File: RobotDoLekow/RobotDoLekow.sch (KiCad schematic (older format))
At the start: 24 parts, among them M1 Stepper_Motor_unipolar_5pin, Q1 2N3904, SW1 SW_Push_LED, U1 Converter_module, U2 RTC_module_DS1307, U3 ESP8266_module, U4 Driver_module_ULN2003

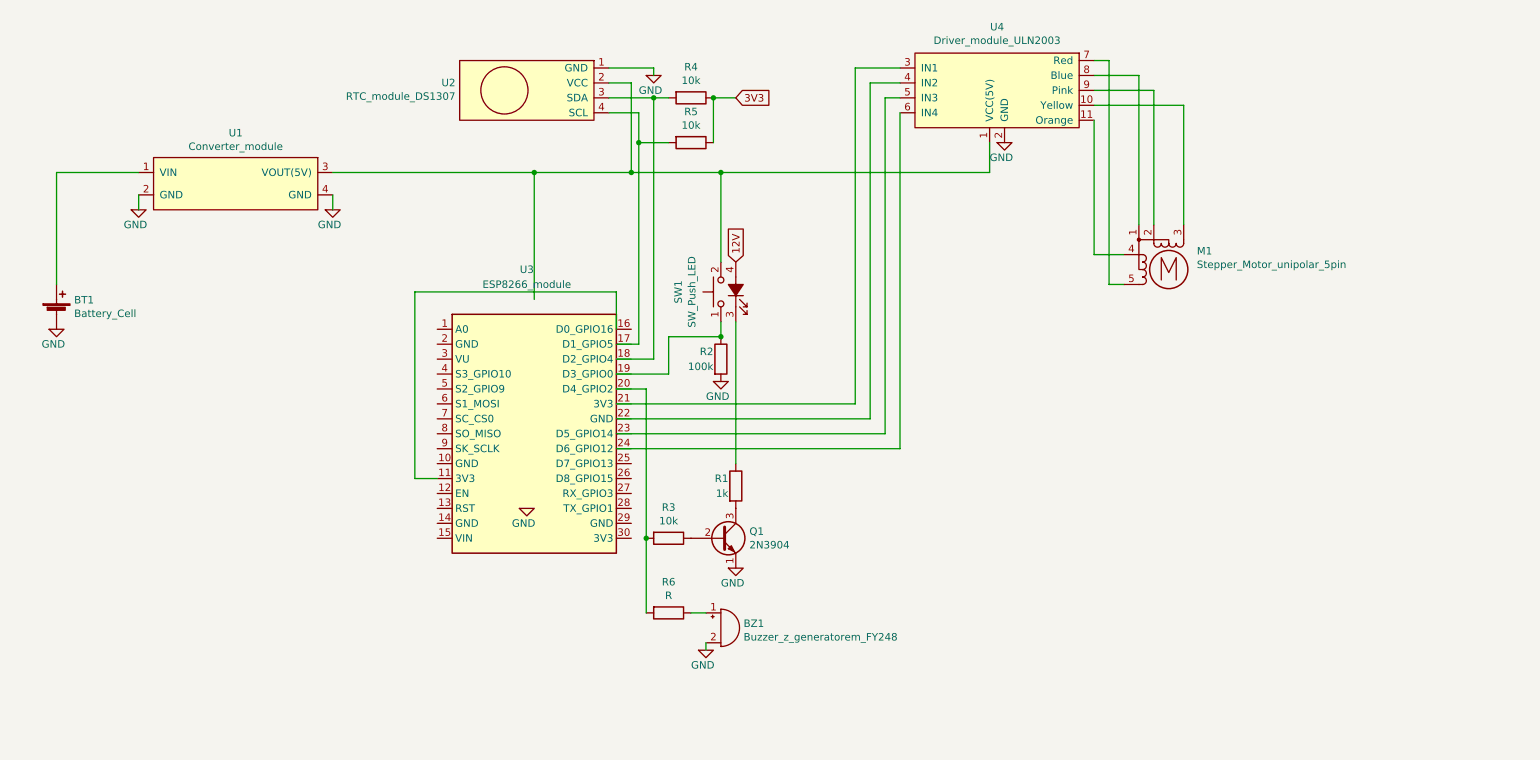
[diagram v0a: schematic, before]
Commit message: dodawanie ekspandera
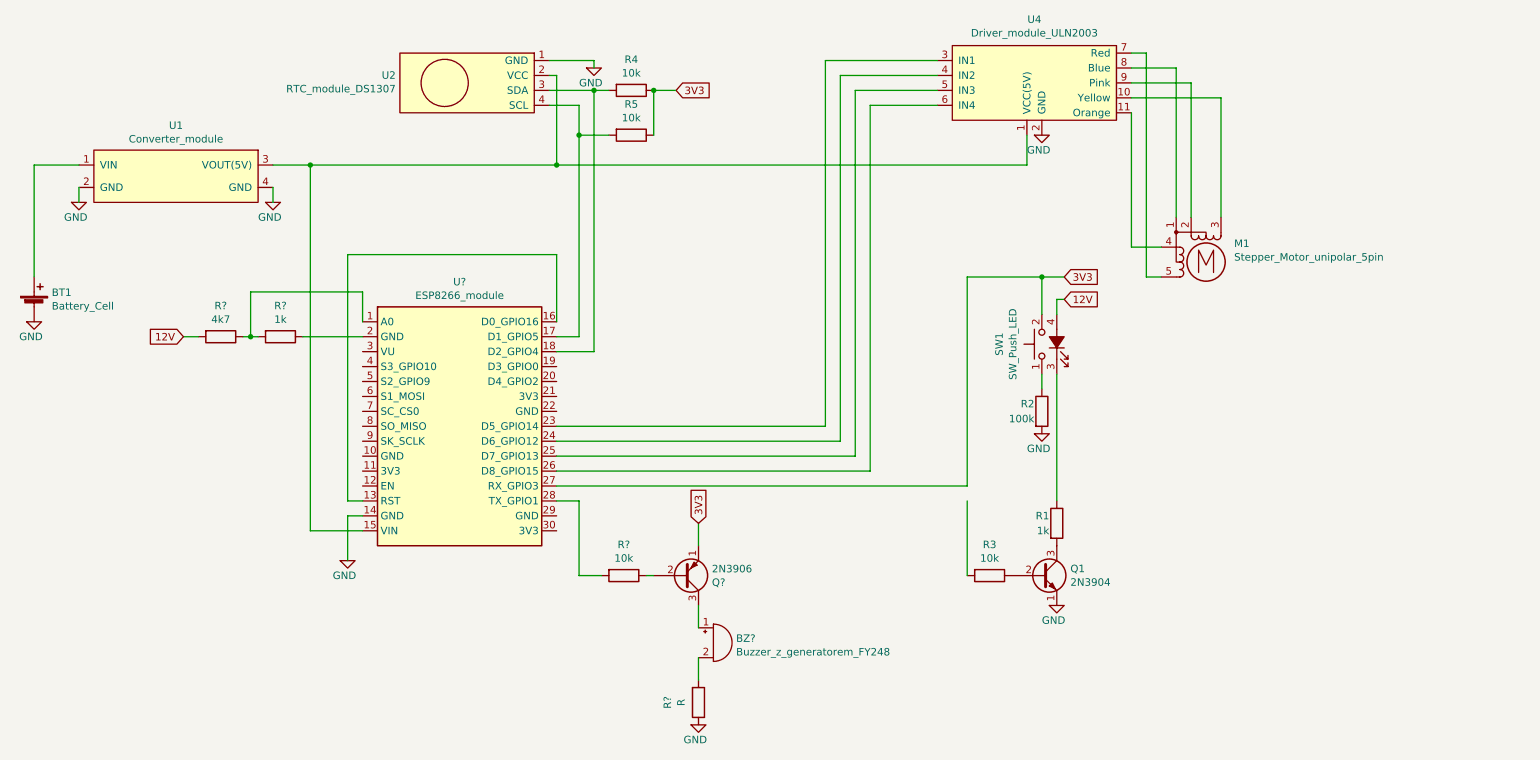
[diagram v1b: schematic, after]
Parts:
- removed BZ1: Buzzer_z_generatorem_FY248, symbol Device:Buzzer
- removed R6: R, symbol Device:R
- removed U3: ESP8266_module, RF_Module:ESP-12E, symbol New_LibraryKiCad:ESP8266_module
- added BZ?: Buzzer_z_generatorem_FY248, symbol Device:Buzzer
- added Q?: 2N3906, Package_TO_SOT_THT:TO-92_Inline, symbol Transistor_BJT:2N3906
- added R?: R, symbol Device:R
- added R?: 4k7, symbol Device:R
- added R?: 1k, symbol Device:R
- added R?: 10k, symbol Device:R
- added U?: ESP8266_module, RF_Module:ESP-12E, symbol New_LibraryKiCad:ESP8266_module
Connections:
- wire segments 62 -> 78
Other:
- moved on the sheet: BT1, M1, Q1, R1, R2, R3, R4, R5, SW1, U1, U2, U4

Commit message: poprawienie aplikacji mobilnej i rozwijanie kodu do esp8266
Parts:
- removed GND (x2): 0, symbol pspice:0
- removed Q?: 2N3906, Package_TO_SOT_THT:TO-92_Inline, symbol Transistor_BJT:2N3906
- removed R?: 10k, symbol Device:R
- removed U1: Converter_module, symbol New_LibraryKiCad:Converter_module
- added GND: 0, symbol pspice:0
- added U5: PCF8574N, symbol New_LibraryKiCad:PCF8574N
- gave numbers to parts that had none: 1
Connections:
- net 0: now also BZ?.2 (+), GND.1 (0), U5.1 (A0), U5.2 (A1), U5.3 (A2), U5.8 (VSS); no longer R?.1
- net 3V3: now also U5.6 (P2); no longer U3.27 (RX_GPIO3)
- net at U2.2 (VCC), U3.15 (VIN), U4.1 (VCC(5V)): now also BT1.1 (+), R?.2
- net at R4.2, U2.3 (SDA), U3.18 (D2_GPIO4): now also U5.15 (SDA)
- net at R5.2, U2.4 (SCL), U3.17 (D1_GPIO5): now also U5.14 (SCL)
- net at U4.3 (IN1): now also U5.9 (P4); no longer U3.23 (D5_GPIO14)
- net at U4.4 (IN2): now also U5.10 (P5); no longer U3.24 (D6_GPIO12)
- net at U4.5 (IN3): now also U5.11 (P6); no longer U3.25 (D7_GPIO13)
- net at U4.6 (IN4): now also U5.12 (P7); no longer U3.26 (D8_GPIO15)
- net at R3.2: now also U5.5 (P1)
- net at U3.21 (3V3): now also U5.16 (VDD)
- net at R?.2: now also U5.4 (P0); no longer BZ?.2 (+)
- net at BZ?.1 (-): now also R?.1
- net 12V renamed 5V
- net 5V: no longer R?.2
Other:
- moved on the sheet: BT1, BZ?, Q1, R1, R2, R3, R?, SW1

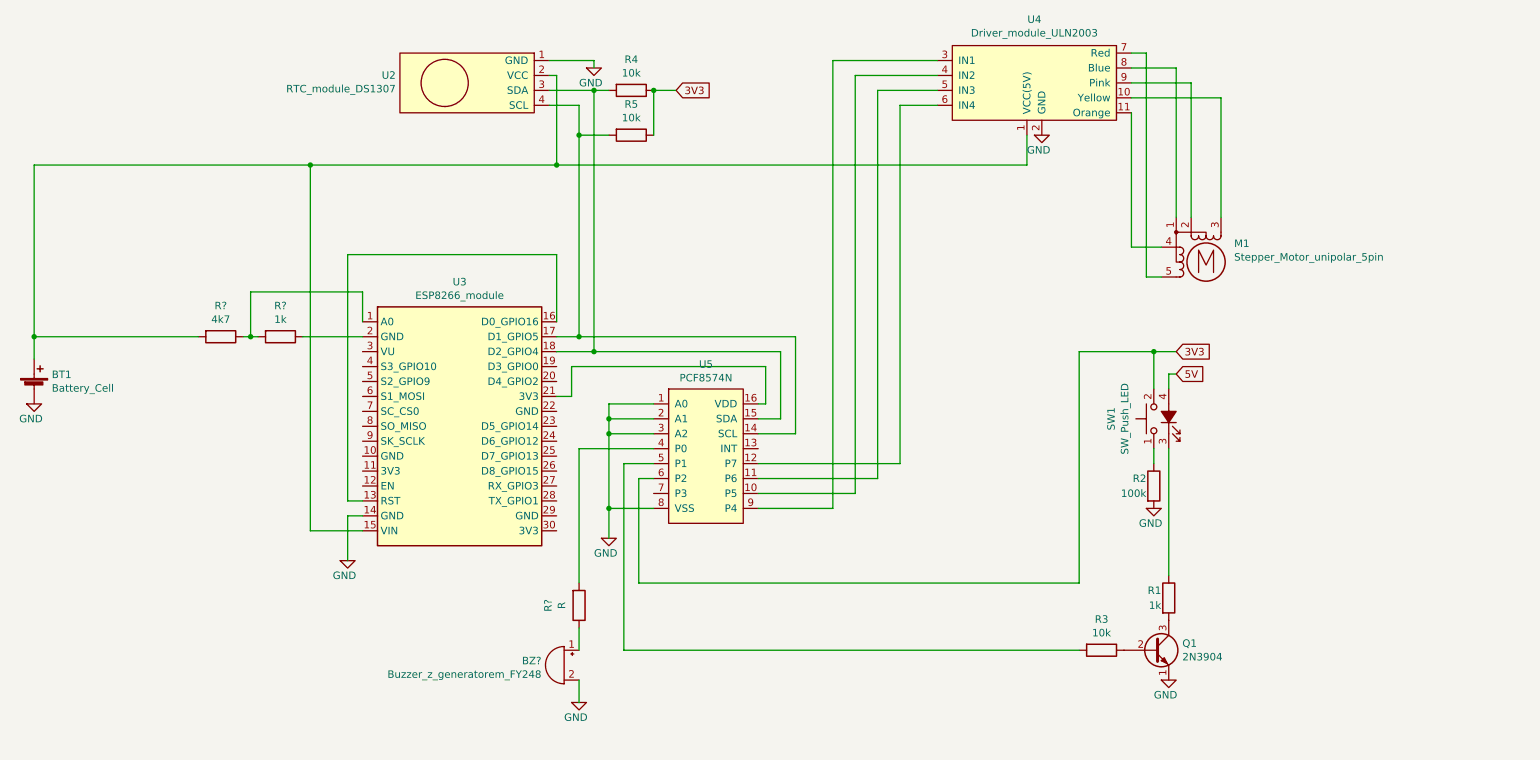
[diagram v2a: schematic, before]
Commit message: poprawienie pobierania nastepnego alarmu oraz nazewnictwa liczbowego
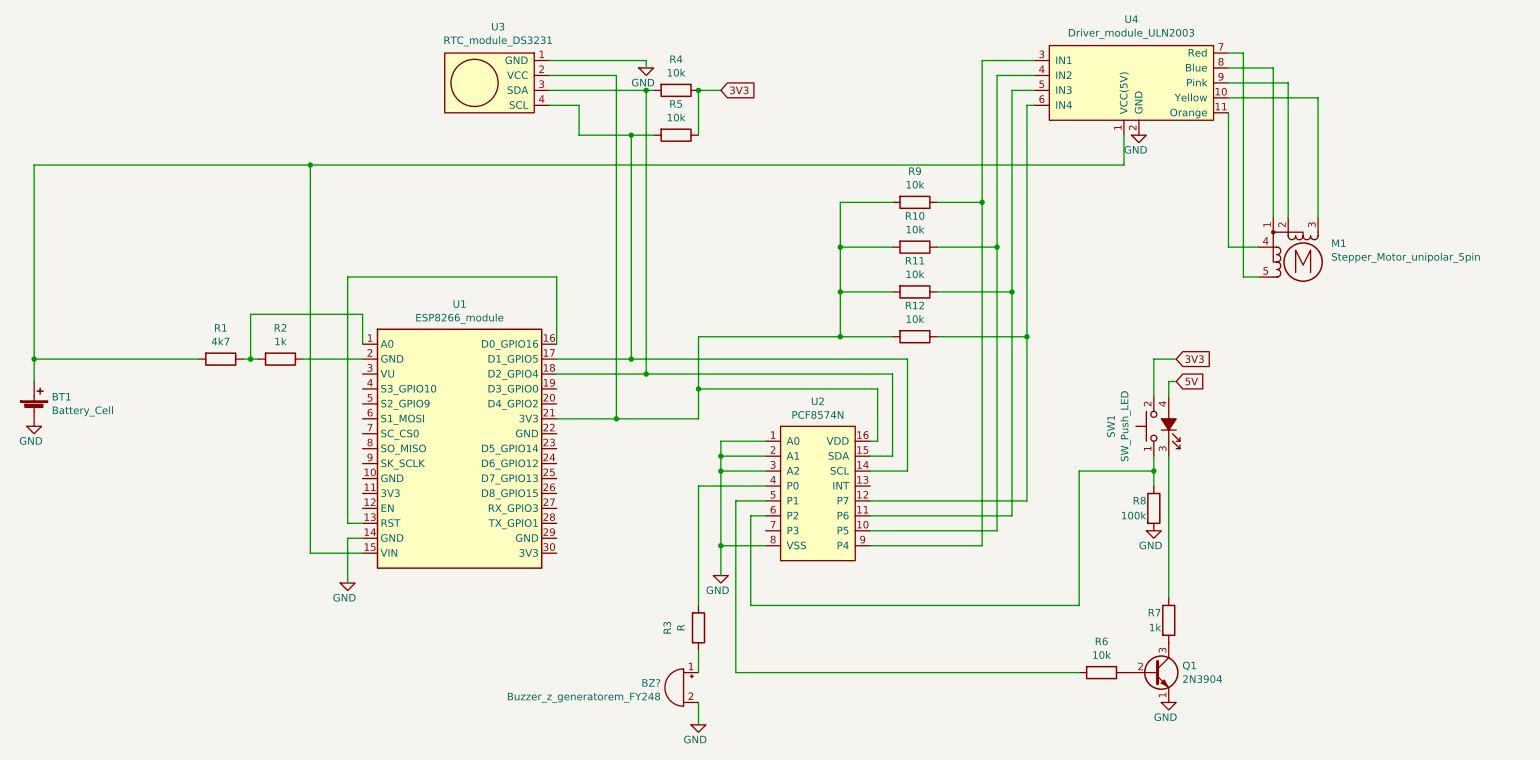
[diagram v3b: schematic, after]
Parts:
- removed U2: RTC_module_DS1307, symbol New_LibraryKiCad:RTC_module_DS1307
- added R10, R11, R12, R9: 10k, symbol Device:R
- added U3: RTC_module_DS3231, symbol New_LibraryKiCad:RTC_module_DS3231
- gave numbers to parts that had none: 3
- renumbered R3 to R6, R1 to R7, R2 to R8, U3 to U1, U5 to U2
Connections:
- net 0: now also U3.1 (GND)
- net 3V3: no longer U2.6 (P2)
- net at R4.2, U1.18 (D2_GPIO4), U2.15 (SDA): now also U3.3 (SDA)
- net at R5.2, U1.17 (D1_GPIO5), U2.14 (SCL): now also U3.4 (SCL)
- net at U2.9 (P4), U4.3 (IN1): now also R9.1
- net at U2.10 (P5), U4.4 (IN2): now also R10.1
- net at U2.11 (P6), U4.5 (IN3): now also R11.1
- net at U2.12 (P7), U4.6 (IN4): now also R12.1
- net at R8.1, SW1.1: now also U2.6 (P2)
- net at U1.21 (3V3), U2.16 (VDD): now also R10.2, R11.2, R12.2, R9.2, U3.2 (VCC)
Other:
- moved on the sheet: BT1, BZ?, M1, Q1, R1, R2, R3, R4, R5, R6, R7, R8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

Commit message: wersja końcowa
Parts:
- removed BT1: Battery_Cell, symbol Device:Battery_Cell
- removed R1: 4k7, symbol Device:R
- removed R2: 1k, symbol Device:R
- added U5: power_supply, symbol New_LibraryKiCad:power_supply
- R8: value 100k -> 10k
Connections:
- net 0: now also U5.0
- net at U1.15 (VIN), U4.1 (VCC(5V)): now also U5.0
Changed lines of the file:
@@
 Comment4 ""
 $EndDescr
-$Comp
-L Device:Battery_Cell BT1
-U 1 1 5F5E72F1
-P 1400 4400
-F 0 "BT1" H 1518 4496 50  0000 L CNN
-F 1 "Battery_Cell" H 1518 4405 50  0000 L CNN
-F 2 "" V 1400 4460 50  0001 C CNN
-F 3 "~" V 1400 4460 50  0001 C CNN
-	1    1400 4400
-	1    0    0    -1
-$EndComp
 Wire Wire Line
 	8700 2550 8700 2750
@@
 L pspice:0 GND
 U 1 1 5F63417C
-P 1400 4500
-F 0 "GND" H 1300 4400 50  0000 L CNN
-F 1 "0" H 1400 4589 50  0001 C CNN
-F 2 "" H 1400 4500 50  0001 C CNN
-F 3 "~" H 1400 4500 50  0001 C CNN
-	1    1400 4500
+P 1400 3850
+F 0 "GND" H 1300 3750 50  0000 L CNN
+F 1 "0" H 1400 3939 50  0001 C CNN
+F 2 "" H 1400 3850 50  0001 C CNN
+F 3 "~" H 1400 3850 50  0001 C CNN
+	1    1400 3850
 	1    0    0    -1
 $EndComp
@@
 P 8900 5050
 F 0 "R8" H 8850 5100 50  0000 R CNN
-F 1 "100k" H 8850 5000 50  0000 R CNN
+F 1 "10k" H 8850 5000 50  0000 R CNN
 F 2 "" V 8830 5050 50  0001 C CNN
 F 3 "~" H 8900 5050 50  0001 C CNN
@@
 	3250 5350 3600 5350
 $Comp
-L Device:R R1
-U 1 1 5FAA4304
-P 2650 4050
-F 0 "R1" V 2443 4050 50  0000 C CNN
-F 1 "4k7" V 2534 4050 50  0000 C CNN
-F 2 "" V 2580 4050 50  0001 C CNN
-F 3 "~" H 2650 4050 50  0001 C CNN
-	1    2650 4050
-	0    1    1    0
-$EndComp
-$Comp
-L Device:R R2
-U 1 1 5FAA6AC3
-P 3050 4050
-F 0 "R2" V 2843 4050 50  0000 C CNN
-F 1 "1k" V 2934 4050 50  0000 C CNN
-F 2 "" V 2980 4050 50  0001 C CNN
-F 3 "~" H 3050 4050 50  0001 C CNN
-	1    3050 4050
-	0    1    1    0
-$EndComp
-Wire Wire Line
-	2800 4050 2850 4050
-Wire Wire Line
-	3200 4050 3600 4050
-Wire Wire Line
-	3600 3750 2850 3750
-Connection ~ 2850 4050
-Wire Wire Line
-	2850 4050 2900 4050
-Wire Wire Line
-	3600 3750 3600 3950
-Wire Wire Line
-	2850 3750 2850 4050
-$Comp
 L pspice:0 GND
 U 1 1 5FADE33E
@@
 	6300 4900 5850 4900
 Wire Wire Line
-	1400 4050 1400 4200
-Wire Wire Line
 	6300 5000 6100 5000
 Wire Wire Line
@@
 Wire Wire Line
 	6200 5100 6300 5100
-Wire Wire Line
-	1400 4050 2500 4050
-Connection ~ 1400 4050
 Wire Wire Line
 	7000 4600 7050 4600
@@
 Wire Wire Line
 	1400 2750 3250 2750
-Wire Wire Line
-	1400 2750 1400 4050
 Wire Wire Line
 	3250 2750 3250 5350
@@
 Wire Wire Line
 	8050 3900 8050 5000
+Wire Wire Line
+	1400 3850 1400 3700
+$Comp
+L New_LibraryKiCad:power_supply U5
+U 1 1 5FBFAB08
+P 1400 3400
+F 0 "U5" H 1578 3296 50  0000 L CNN
+F 1 "power_supply" H 1578 3205 50  0000 L CNN
+F 2 "" H 1350 3500 50  0001 C CNN
+F 3 "" H 1350 3500 50  0001 C CNN
+	1    1400 3400
+	1    0    0    -1
+$EndComp
+Wire Wire Line
+	1400 2750 1400 3400
 $EndSCHEMATC
